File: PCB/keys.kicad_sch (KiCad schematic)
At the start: 106 parts, among them SW1 Esc, SW10 F9, SW100 Steuerung, SW101 ←, SW102 ↓, SW103 →, SW104 0, SW105 Komma, SW106 Eingabe, SW11 F10, SW12 F11, SW13 F12, SW14 Druck, SW15 Rollen, SW16 Pause, SW17 Sperren, SW18 Zirkumflex, SW19 1, SW2 F1, SW20 2, SW21 3, SW22 4, SW23 5, SW24 6, SW25 7, SW26 8, SW27 9, SW28 0, SW29 Eszett, SW3 F2, SW30 Akut, SW31 Rücktaste, SW32 Einfügen, SW33 Pos1, SW34 Bild↑, SW35 NumLock, SW36 Schrägstrich, SW37 Sternchen, SW38 Minus, SW39 Tab, SW4 F3, SW40 Q, SW41 W, SW42 E, SW43 R, SW44 T, SW45 Z, SW46 U, SW47 I, SW48 O, SW49 P, SW5 F4, SW50 Ü, SW51 Plus, SW52 Eingabe, SW53 Entfernen, SW54 Ende, SW55 Bild↓, SW56 7, SW57 8, SW58 9, SW59 Compose, SW6 F5, SW60 A, SW61 S, SW62 D, SW63 F, SW64 G, SW65 H, SW66 J, SW67 K, SW68 L, SW69 Ö, SW7 F6, SW70 Ä, SW71 Raute, SW72 4, SW73 5, SW74 6, SW75 Plus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

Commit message: Add power supplies
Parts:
- SW1: value Esc -> ~; Key (none) -> Esc
- SW10: value F9 -> ~; Key (none) -> F9
- SW100, SW93: value Steuerung -> ~; Key (none) -> Steuerung
- SW101: value ← -> ~; Key (none) -> ←
- SW102: value ↓ -> ~; Key (none) -> ↓
- SW103: value → -> ~; Key (none) -> →
- SW104, SW28: value 0 -> ~; Key (none) -> 0
- SW105, SW85: value Komma -> ~; Key (none) -> Komma
- SW106, SW52: value Eingabe -> ~; Key (none) -> Eingabe
- SW11: value F10 -> ~; Key (none) -> F10
- SW12: value F11 -> ~; Key (none) -> F11
- SW13: value F12 -> ~; Key (none) -> F12
- SW14: value Druck -> ~; Key (none) -> Druck
- SW15: value Rollen -> ~; Key (none) -> Rollen
- SW16: value Pause -> ~; Key (none) -> Pause
- SW17: value Sperren -> ~; Key (none) -> Sperren
- SW18: value Zirkumflex -> ~; Key (none) -> Zirkumflex
- SW19, SW90: value 1 -> ~; Key (none) -> 1
- SW2: value F1 -> ~; Key (none) -> F1
- SW20, SW91: value 2 -> ~; Key (none) -> 2
- SW21, SW92: value 3 -> ~; Key (none) -> 3
- SW22, SW72: value 4 -> ~; Key (none) -> 4
- SW23, SW73: value 5 -> ~; Key (none) -> 5
- SW24, SW74: value 6 -> ~; Key (none) -> 6
- SW25, SW56: value 7 -> ~; Key (none) -> 7
- SW26, SW57: value 8 -> ~; Key (none) -> 8
- SW27, SW58: value 9 -> ~; Key (none) -> 9
- SW29: value Eszett -> ~; Key (none) -> Eszett
- SW3: value F2 -> ~; Key (none) -> F2
- SW30: value Akut -> ~; Key (none) -> Akut
- SW31: value Rücktaste -> ~; Key (none) -> Rücktaste
- SW32: value Einfügen -> ~; Key (none) -> Einfügen
- SW33: value Pos1 -> ~; Key (none) -> Pos1
- SW34: value Bild↑ -> ~; Key (none) -> Bild↑
- SW35: value NumLock -> ~; Key (none) -> NumLock
- SW36: value Schrägstrich -> ~; Key (none) -> Schrägstrich
- SW37: value Sternchen -> ~; Key (none) -> Sternchen
- SW38, SW87: value Minus -> ~; Key (none) -> Minus
- SW39: value Tab -> ~; Key (none) -> Tab
- SW4: value F3 -> ~; Key (none) -> F3
- SW40: value Q -> ~; Key (none) -> Q
- SW41: value W -> ~; Key (none) -> W
- SW42: value E -> ~; Key (none) -> E
- SW43: value R -> ~; Key (none) -> R
- SW44: value T -> ~; Key (none) -> T
- SW45: value Z -> ~; Key (none) -> Z
- SW46: value U -> ~; Key (none) -> U
- SW47: value I -> ~; Key (none) -> I
- SW48: value O -> ~; Key (none) -> O
- SW49: value P -> ~; Key (none) -> P
- SW5: value F4 -> ~; Key (none) -> F4
- SW50: value Ü -> ~; Key (none) -> Ü
- SW51, SW75: value Plus -> ~; Key (none) -> Plus
- SW53: value Entfernen -> ~; Key (none) -> Entfernen
- SW54: value Ende -> ~; Key (none) -> Ende
- SW55: value Bild↓ -> ~; Key (none) -> Bild↓
- SW59: value Compose -> ~; Key (none) -> Compose
- SW6: value F5 -> ~; Key (none) -> F5
- SW60: value A -> ~; Key (none) -> A
- SW61: value S -> ~; Key (none) -> S
- SW62: value D -> ~; Key (none) -> D
- SW63: value F -> ~; Key (none) -> F
- SW64: value G -> ~; Key (none) -> G
- SW65: value H -> ~; Key (none) -> H
- SW66: value J -> ~; Key (none) -> J
- SW67: value K -> ~; Key (none) -> K
- SW68: value L -> ~; Key (none) -> L
- SW69: value Ö -> ~; Key (none) -> Ö
- SW7: value F6 -> ~; Key (none) -> F6
- SW70: value Ä -> ~; Key (none) -> Ä
- SW71: value Raute -> ~; Key (none) -> Raute
- SW76, SW88: value Umschalt -> ~; Key (none) -> Umschalt
- SW77: value < -> ~; Key (none) -> <
- SW78: value Y -> ~; Key (none) -> Y
- SW79: value X -> ~; Key (none) -> X
- SW8: value F7 -> ~; Key (none) -> F7
- SW80: value C -> ~; Key (none) -> C
- SW81: value V -> ~; Key (none) -> V
- SW82: value B -> ~; Key (none) -> B
- SW83: value N -> ~; Key (none) -> N
- SW84: value M -> ~; Key (none) -> M
- SW86: value Punkt -> ~; Key (none) -> Punkt
- SW89: value ↑ -> ~; Key (none) -> ↑
- SW9: value F8 -> ~; Key (none) -> F8
- SW94, SW98: value Meta -> ~; Key (none) -> Meta
- SW95: value Alt -> ~; Key (none) -> Alt
- SW96: value Leertaste -> ~; Key (none) -> Leertaste
- SW97: value AltGr -> ~; Key (none) -> AltGr
- SW99: value Menü -> ~; Key (none) -> Menü

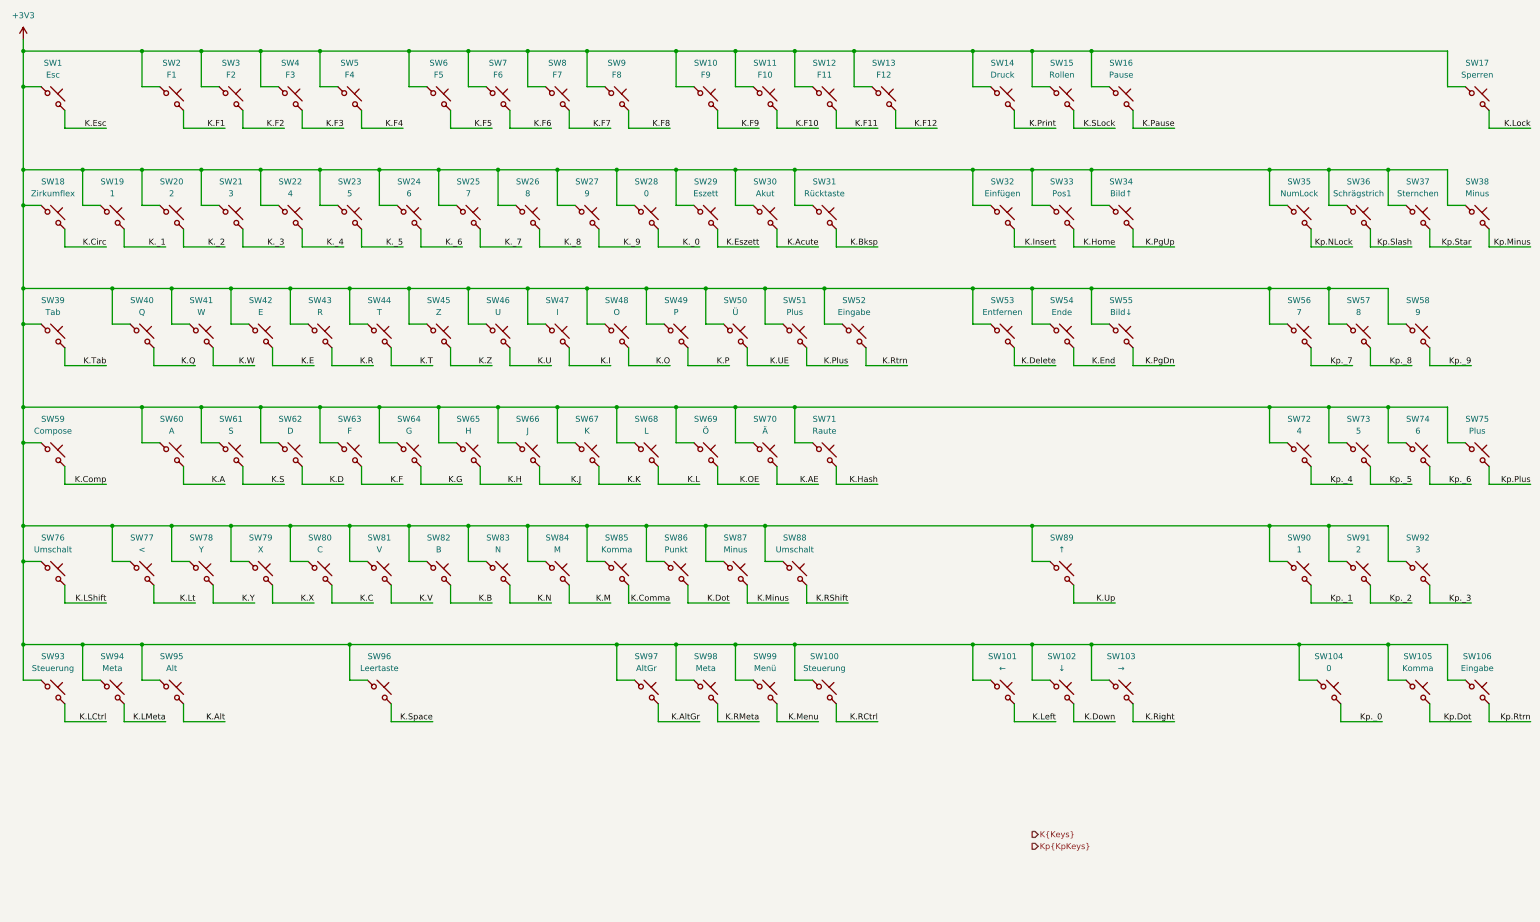
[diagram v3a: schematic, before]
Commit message: Add the USB to JTAG bridge
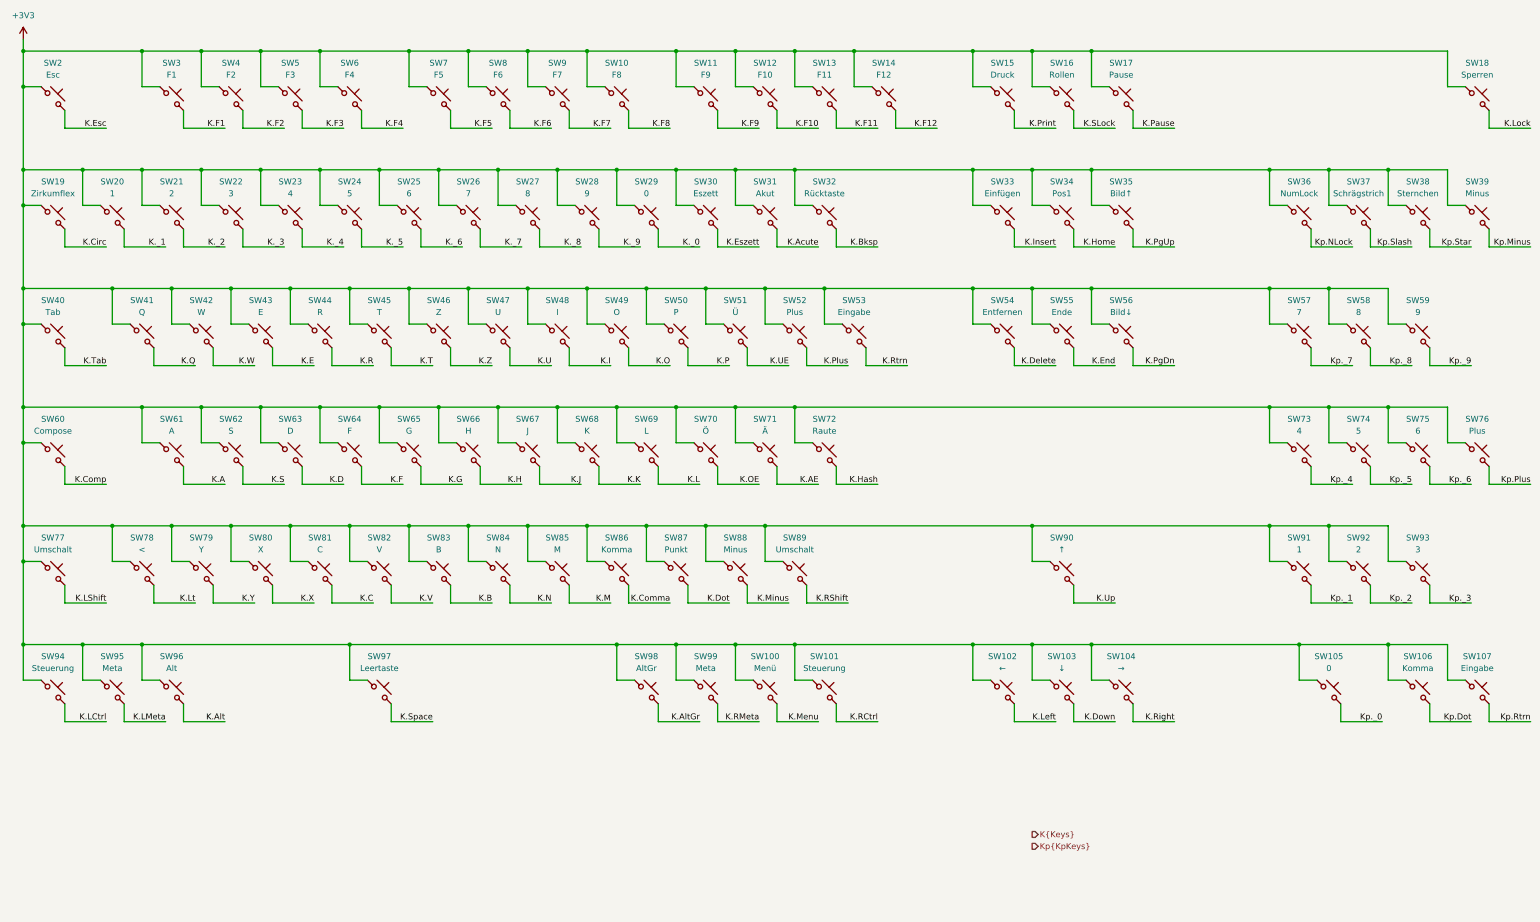
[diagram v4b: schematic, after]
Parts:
- renumbered SW9 to SW10, SW99 to SW100, SW100 to SW101, SW101 to SW102, SW102 to SW103, SW103 to SW104, SW104 to SW105, SW105 to SW106, SW106 to SW107, SW10 to SW11, SW11 to SW12, SW12 to SW13, SW13 to SW14, SW14 to SW15, SW15 to SW16, SW16 to SW17, SW17 to SW18, SW18 to SW19, SW1 to SW2, SW19 to SW20, SW20 to SW21, SW21 to SW22, SW22 to SW23, SW23 to SW24, SW24 to SW25, SW25 to SW26, SW26 to SW27, SW27 to SW28, SW28 to SW29, SW2 to SW3, SW29 to SW30, SW30 to SW31, SW31 to SW32, SW32 to SW33, SW33 to SW34, SW34 to SW35, SW35 to SW36, SW36 to SW37, SW37 to SW38, SW38 to SW39, SW3 to SW4, SW39 to SW40, SW40 to SW41, SW41 to SW42, SW42 to SW43, SW43 to SW44, SW44 to SW45, SW45 to SW46, SW46 to SW47, SW47 to SW48, SW48 to SW49, SW4 to SW5, SW49 to SW50, SW50 to SW51, SW51 to SW52, SW52 to SW53, SW53 to SW54, SW54 to SW55, SW55 to SW56, SW56 to SW57, SW57 to SW58, SW58 to SW59, SW5 to SW6, SW59 to SW60, SW60 to SW61, SW61 to SW62, SW62 to SW63, SW63 to SW64, SW64 to SW65, SW65 to SW66, SW66 to SW67, SW67 to SW68, SW68 to SW69, SW6 to SW7, SW69 to SW70, SW70 to SW71, SW71 to SW72, SW72 to SW73, SW73 to SW74, SW74 to SW75, SW75 to SW76, SW76 to SW77, SW77 to SW78, SW78 to SW79, SW7 to SW8, SW79 to SW80, SW80 to SW81, SW81 to SW82, SW82 to SW83, SW83 to SW84, SW84 to SW85, SW85 to SW86, SW86 to SW87, SW87 to SW88, SW88 to SW89, SW8 to SW9, SW89 to SW90, SW90 to SW91, SW91 to SW92, SW92 to SW93, SW93 to SW94, SW94 to SW95, SW95 to SW96, SW96 to SW97, SW97 to SW98, SW98 to SW99

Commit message: Improve the CH347F schematics and added 3D models
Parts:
- SW10, SW102, SW103, SW104, SW106, SW11, SW12, SW13, SW14, SW15, SW16, SW17, SW18, SW19, SW2, SW20, SW21, SW22, SW23, SW24, SW25, SW26, SW27, SW28, SW29, SW3, SW30, SW31, SW33, SW34, SW35, SW36, SW37, SW38, SW39, SW4, SW41, SW42, SW43, SW44, SW45, SW46, SW47, SW48, SW49, SW5, SW50, SW51, SW52, SW54, SW55, SW56, SW57, SW58, SW59, SW6, SW61, SW62, SW63, SW64, SW65, SW66, SW67, SW68, SW69, SW7, SW70, SW71, SW72, SW73, SW74, SW75, SW78, SW79, SW8, SW80, SW81, SW82, SW83, SW84, SW85, SW86, SW87, SW88, SW9, SW90, SW91, SW92, SW93: footprint Button_Switch_Keyboard:SW_Cherry_MX_1.00u_PCB -> clavier:SW_Cherry_MX_1.00u_PCB
- SW100, SW101, SW77, SW94, SW95, SW96, SW98, SW99: footprint Button_Switch_Keyboard:SW_Cherry_MX_1.25u_PCB -> clavier:SW_Cherry_MX_1.25u_PCB
- SW105, SW32: footprint Button_Switch_Keyboard:SW_Cherry_MX_2.00u_PCB -> clavier:SW_Cherry_MX_2.00u_PCB
- SW107, SW76: footprint Button_Switch_Keyboard:SW_Cherry_MX_2.00u_Vertical_PCB -> clavier:SW_Cherry_MX_2.00u_Vertical_PCB
- SW40: footprint Button_Switch_Keyboard:SW_Cherry_MX_1.50u_PCB -> clavier:SW_Cherry_MX_1.50u_PCB
- SW53: footprint Button_Switch_Keyboard:SW_Cherry_MX_ISOEnter_PCB -> clavier:SW_Cherry_MX_ISOEnter_PCB
- SW60: footprint Button_Switch_Keyboard:SW_Cherry_MX_1.75u_PCB -> clavier:SW_Cherry_MX_1.75u_PCB
- SW89: footprint Button_Switch_Keyboard:SW_Cherry_MX_2.75u_PCB -> clavier:SW_Cherry_MX_2.75u_PCB
- SW97: footprint Button_Switch_Keyboard:SW_Cherry_MX_6.25u_PCB -> clavier:SW_Cherry_MX_6.25u_PCB

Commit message: Add LICENSE and minor improvements
- Filled the title blocks
- Connected the LEDs to the FPGA
- Changed the FPGA programming header
- Added USB fuse and capacitors
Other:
- company: (none) -> Copyright (c) 2025 L. Sartory
- title: (none) -> Clavier - Keys
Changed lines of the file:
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@@
 	(generator_version "9.0")
 	(paper "A3")
+	(title_block
+		(title "Clavier - Keys")
+		(date "2025-06-01")
+		(rev "1.0")
+		(company "Copyright (c) 2025 L. Sartory")
+		(comment 1 "SPDX-License-Identifier: CERN-OHL-P-2.0")
+	)
 	(bus_alias "Keys"
 		(members "A" "AE" "Acute" "Alt" "AltGr" "B" "Bksp" "C" "Circ" "Comma" "Comp"
@@
 		(dnp no)
 		(fields_autoplaced yes)
-		(property "Reference" "#PWR068"
+		(property "Reference" "#PWR067"
 			(at 38.1 73.66 0)
 			(effects
@@
 			(project "clavier"
 				(path "/6362c6e0-59ef-40d3-b6e0-7e9dfe7b9b20/fe36ef85-cf96-48c6-8774-50fbc2348e34"
-					(reference "#PWR068")
+					(reference "#PWR067")
 					(unit 1)
 				)

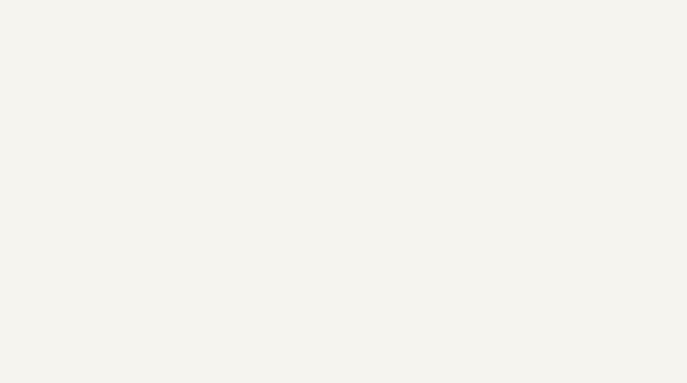
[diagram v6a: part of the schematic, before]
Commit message: Add the first row of keycaps
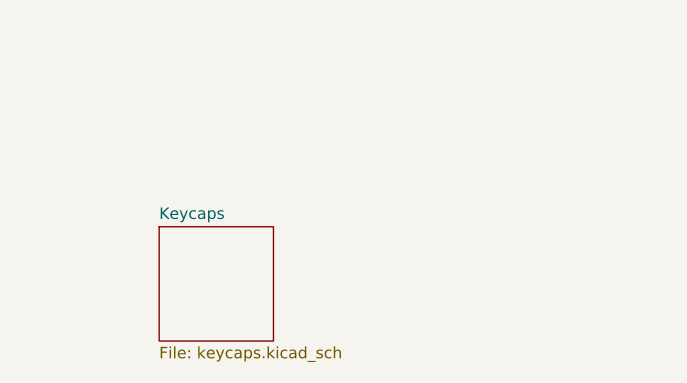
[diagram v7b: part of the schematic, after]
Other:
- added sheet Keycaps (keycaps.kicad_sch)
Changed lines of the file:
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@@
+		)
+	)
+	(sheet
+		(at 50.8 241.3)
+		(size 12.7 12.7)
+		(exclude_from_sim no)
+		(in_bom yes)
+		(on_board yes)
+		(dnp no)
+		(fields_autoplaced yes)
+		(stroke
+			(width 0.1524)
+			(type solid)
+		)
+		(fill
+			(color 0 0 0 0.0000)
+		)
+		(property "Sheetname" "Keycaps"
+			(at 50.8 240.5884 0)
+			(effects
+				(font
+					(size 1.27 1.27)
+				)
+				(justify left bottom)
+			)
+		)
+		(property "Sheetfile" "keycaps.kicad_sch"
+			(at 50.8 254.5846 0)
+			(effects
+				(font
+					(size 1.27 1.27)
+				)
+				(justify left top)
+			)
+		)
+		(instances
+			(project "clavier"
+				(path "/6362c6e0-59ef-40d3-b6e0-7e9dfe7b9b20/fe36ef85-cf96-48c6-8774-50fbc2348e34"
+					(page "8")
+				)
+			)
 		)
 	)
